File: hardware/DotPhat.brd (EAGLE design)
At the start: 30 x 65 mm, 22 parts, among them CN1 1X4-BIG, J2 RASPBERRYPI-40-PIN-GPIO_PTH, J3 USB-MICROB, U1 ATMEGA328P-MU-QFN32, X3 S4B-ZR

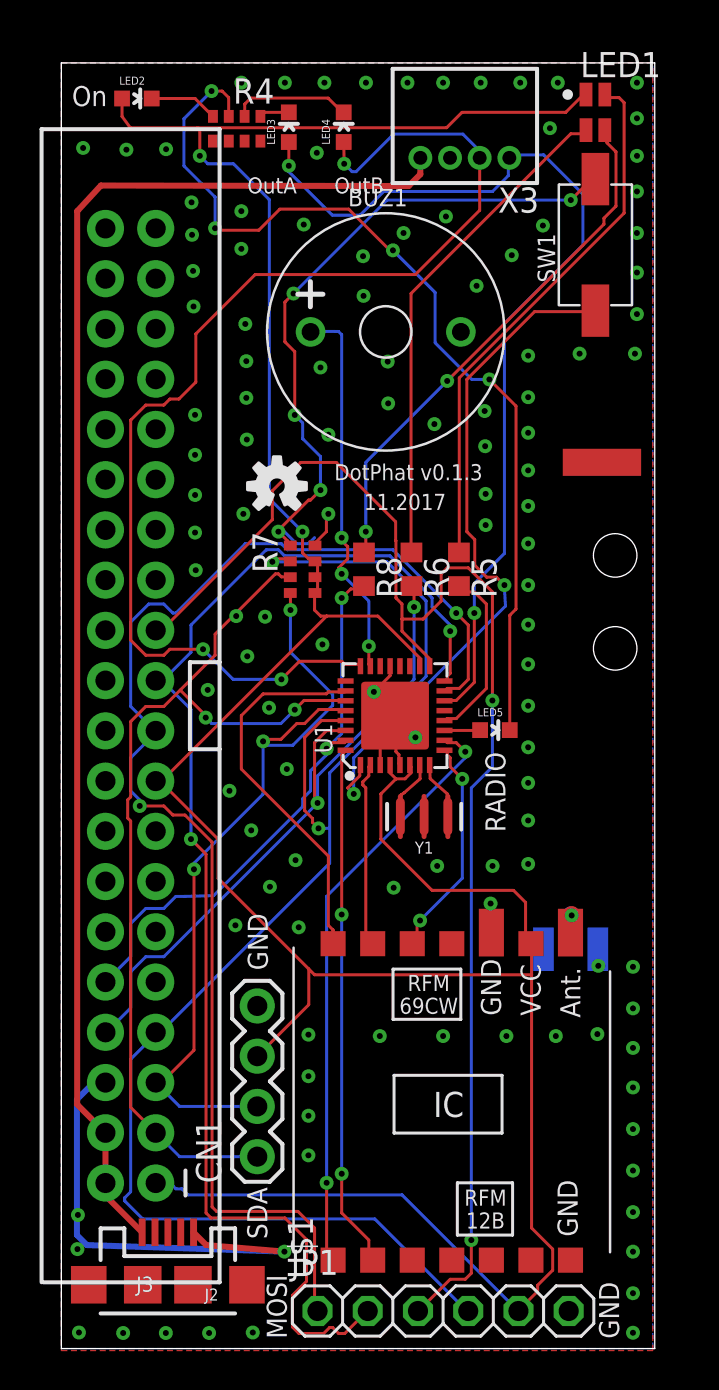
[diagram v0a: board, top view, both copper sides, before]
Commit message: Add HexId, ISM Bands
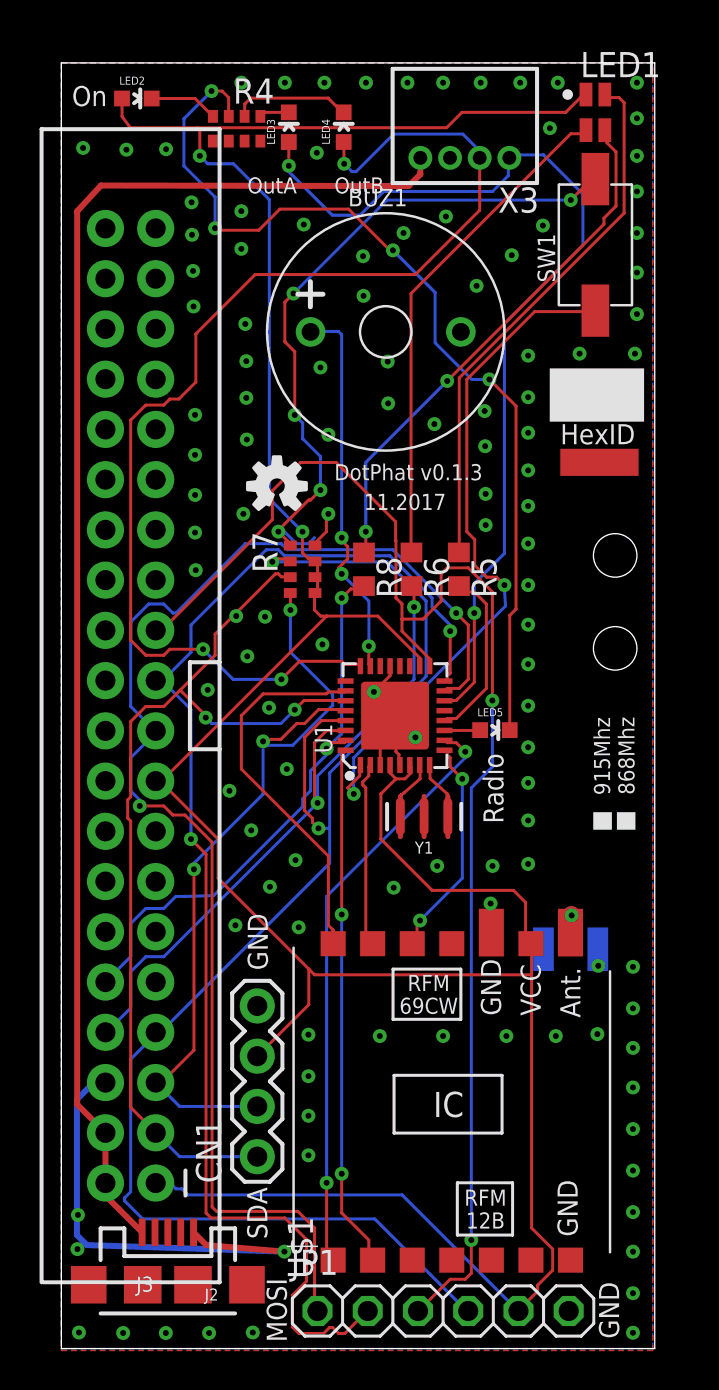
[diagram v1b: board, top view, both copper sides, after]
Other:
- board text added: "868Mhz"
- board text added: "915Mhz"
- board text added: "HexID"
- board text added: "Radio"
- board text removed: "RADIO"

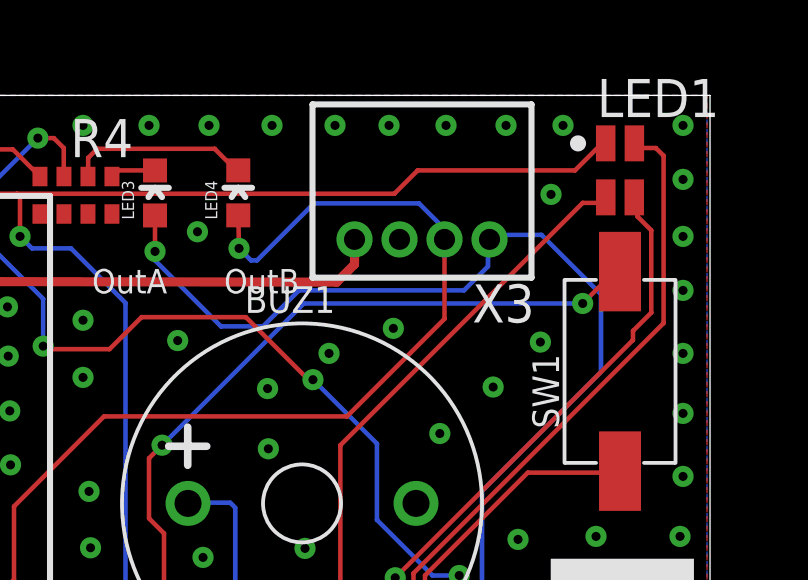
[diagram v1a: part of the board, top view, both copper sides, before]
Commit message: Make JST compatible with generic relays
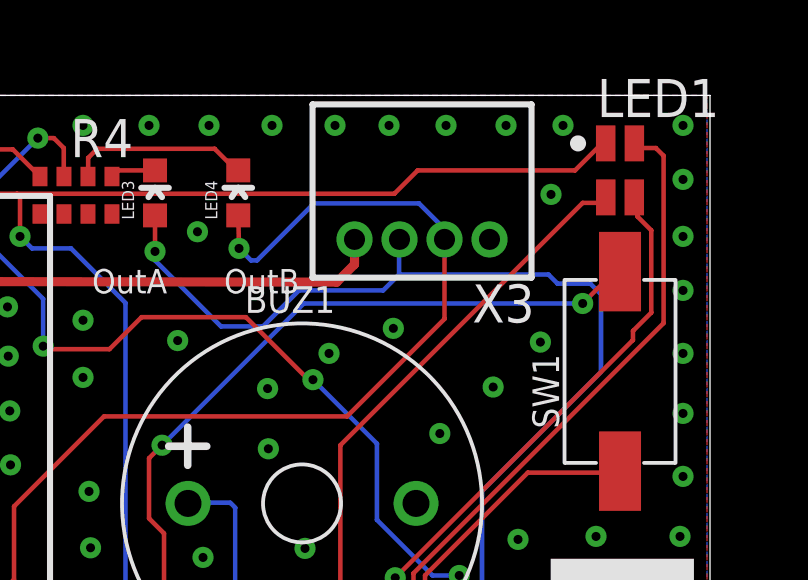
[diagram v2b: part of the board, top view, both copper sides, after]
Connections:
- net GND: now also X3.1; no longer X3.3
- net OUTA: now also X3.3; no longer X3.1

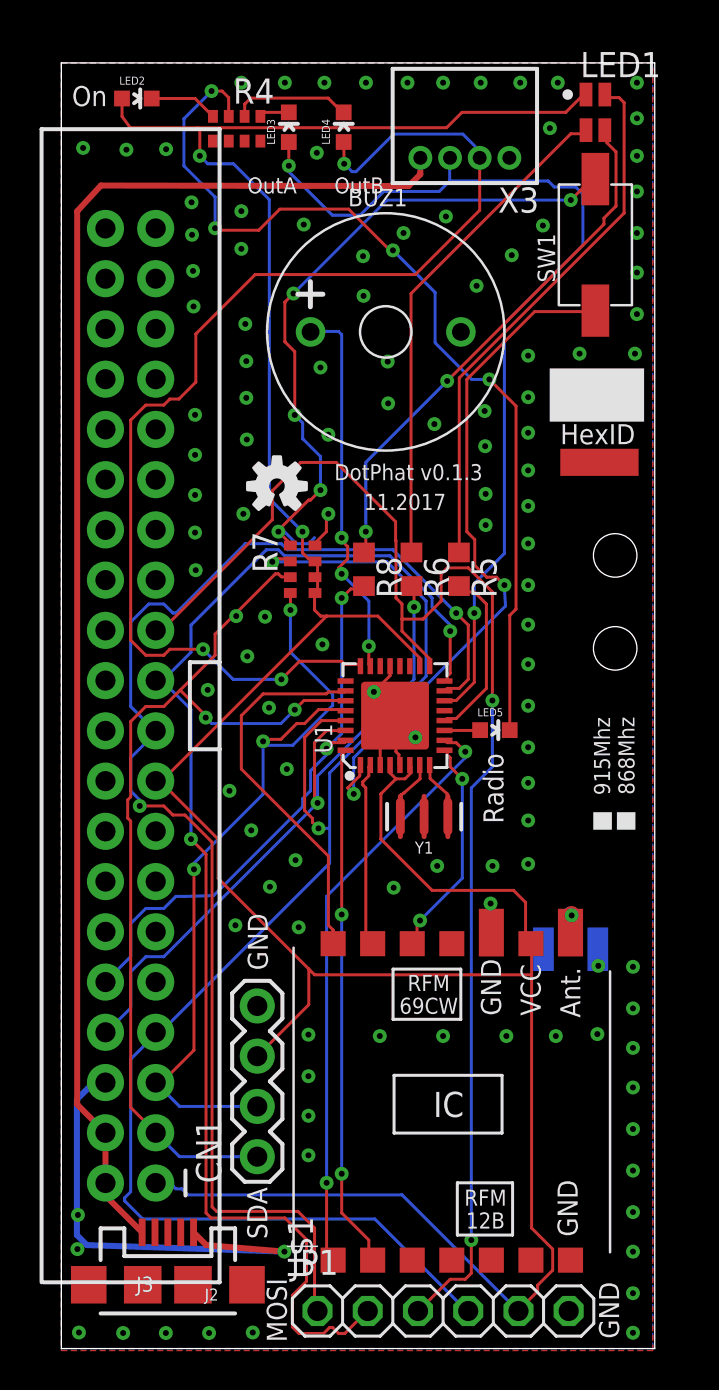
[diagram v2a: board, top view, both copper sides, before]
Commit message: Update with RPi lib with no tPlace
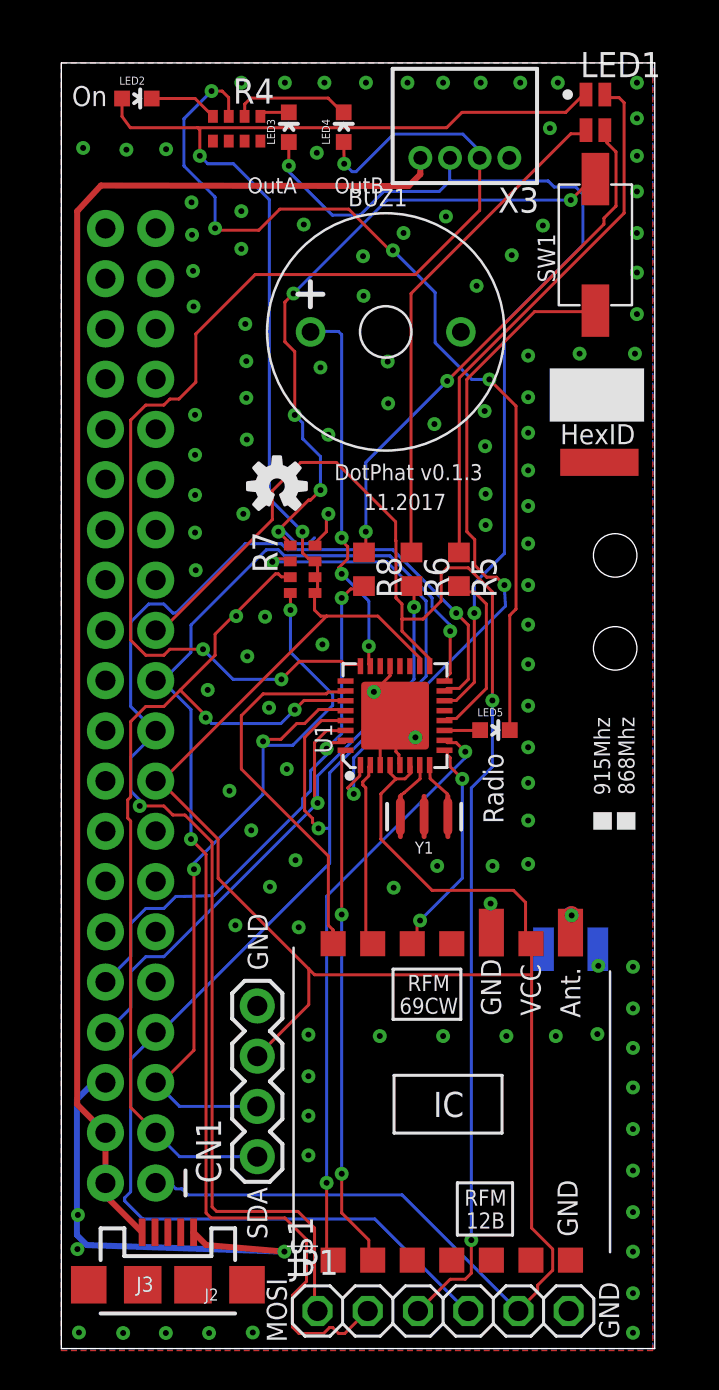
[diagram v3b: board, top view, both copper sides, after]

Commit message: Add mandatory 5V-3.3V capless regulator for USB power
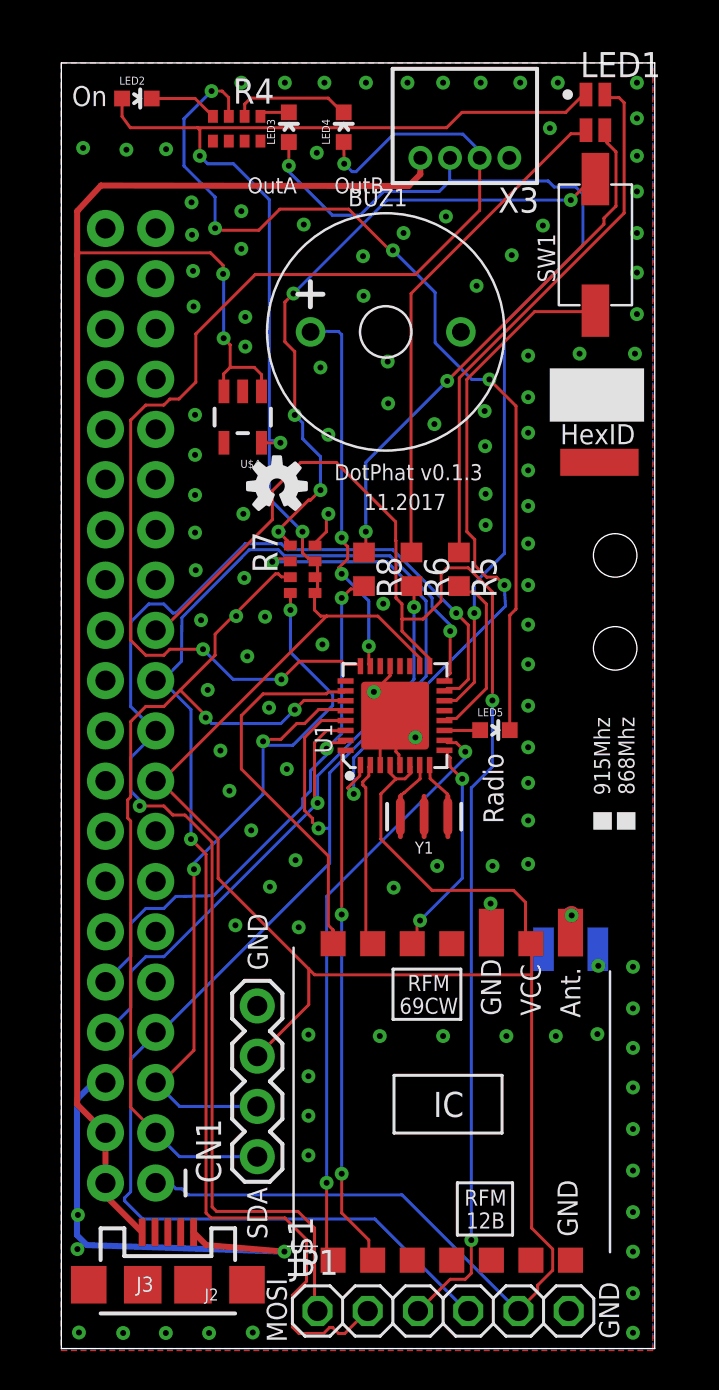
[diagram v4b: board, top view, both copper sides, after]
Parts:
- added U$4: LDCL015, LDCL015:SOT23-5
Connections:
- net +3V3: now also U$4.5
- net +5V: now also U$4.1, U$4.3
- net GND: now also U$4.2
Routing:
- net +5V: track 72.0 -> 88.9 mm, vias 0 -> 2
- net N$5: track 34.8 -> 32.9 mm
- net +3V3: track 159.6 -> 161.2 mm, vias 2 -> 3
- net GND: vias 117 -> 119

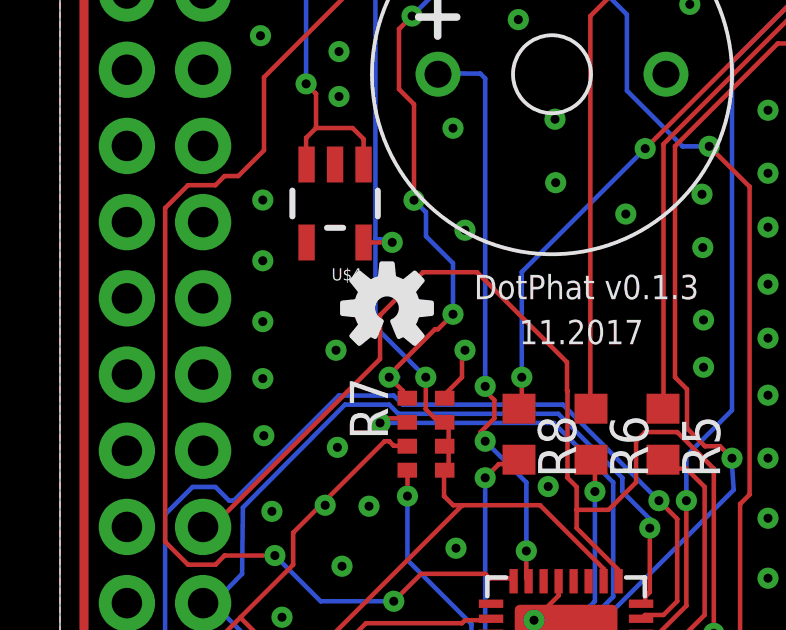
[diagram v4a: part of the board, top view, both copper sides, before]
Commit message: Add filter cap at 3.3V regulator out pin
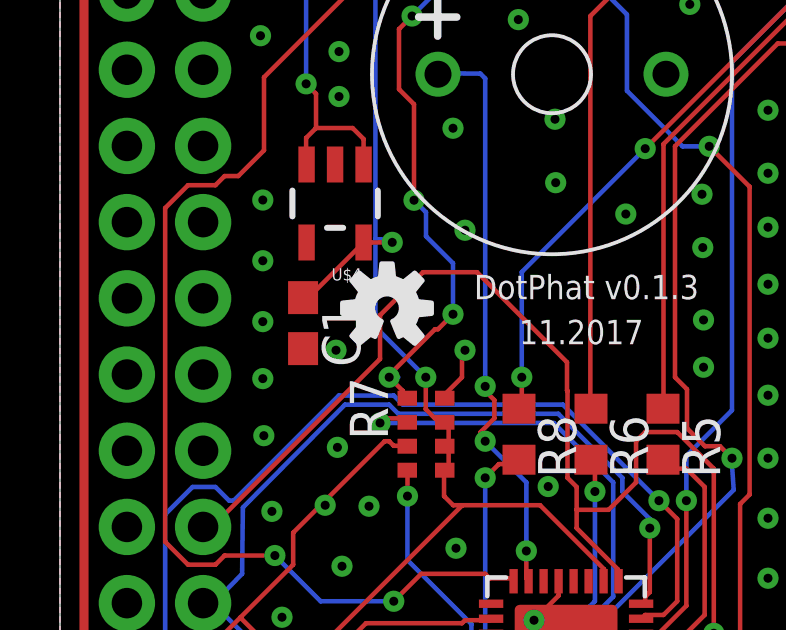
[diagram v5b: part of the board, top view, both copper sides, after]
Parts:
- added C1: (no value), rcl:C0603
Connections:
- net +3V3: now also C1.1
- net GND: now also C1.2
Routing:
- net +3V3: track 161.2 -> 164.0 mm
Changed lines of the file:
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@@
 <grid distance="1" unitdist="mil" unit="mm" style="lines" multiple="1" display="yes" altdistance="0.025" altunitdist="inch" altunit="inch"/>
 <layers>
-<layer number="1" name="Top" color="4" fill="1" visible="no" active="yes"/>
+<layer number="1" name="Top" color="4" fill="1" visible="yes" active="yes"/>
 <layer number="2" name="Route2" color="1" fill="3" visible="no" active="no"/>
 <layer number="3" name="Route3" color="4" fill="3" visible="no" active="no"/>
 <layer number="14" name="Route14" color="1" fill="6" visible="no" active="no"/>
 <layer number="15" name="Route15" color="4" fill="6" visible="no" active="no"/>
-<layer number="16" name="Bottom" color="1" fill="1" visible="no" active="yes"/>
-<layer number="17" name="Pads" color="2" fill="1" visible="no" active="yes"/>
-<layer number="18" name="Vias" color="2" fill="1" visible="no" active="yes"/>
+<layer number="16" name="Bottom" color="1" fill="1" visible="yes" active="yes"/>
+<layer number="17" name="Pads" color="2" fill="1" visible="yes" active="yes"/>
+<layer number="18" name="Vias" color="2" fill="1" visible="yes" active="yes"/>
 <layer number="19" name="Unrouted" color="6" fill="1" visible="yes" active="yes"/>
 <layer number="20" name="Dimension" color="15" fill="1" visible="yes" active="yes"/>
-<layer number="21" name="tPlace" color="7" fill="1" visible="no" active="yes"/>
-<layer number="22" name="bPlace" color="7" fill="1" visible="no" active="yes"/>
-<layer number="23" name="tOrigins" color="15" fill="1" visible="no" active="yes"/>
-<layer number="24" name="bOrigins" color="15" fill="1" visible="no" active="yes"/>
+<layer number="21" name="tPlace" color="7" fill="1" visible="yes" active="yes"/>
+<layer number="22" name="bPlace" color="7" fill="1" visible="yes" active="yes"/>
+<layer number="23" name="tOrigins" color="15" fill="1" visible="yes" active="yes"/>
+<layer number="24" name="bOrigins" color="15" fill="1" visible="yes" active="yes"/>
 <layer number="25" name="tNames" color="7" fill="1" visible="no" active="yes"/>
 <layer number="26" name="bNames" color="7" fill="1" visible="no" active="yes"/>
@@
 <element name="LED5" library="SparkFun" package="LED-0603" value="" x="21.9202" y="31.2674" rot="R270"/>
 <element name="U$4" library="LDCL015" package="SOT23-5" value="LDCL015" x="9.1694" y="47.0916" rot="R180"/>
+<element name="C1" library="rcl" package="C0603" value="" x="8.1026" y="43.1038" rot="R270"/>
 </elements>
 <signals>
@@
 <via x="9.2476" y="38.9624" extent="1-16" drill="0.3"/>
 <via x="16.2734" y="37.6574" extent="1-16" drill="0.3"/>
+<contactref element="C1" pad="2"/>
 </signal>
 <signal name="SDA">
@@
 <wire x1="11.0236" y1="45.7962" x2="11.0236" y2="45.8978" width="0.1524" layer="16"/>
 <wire x1="11.0236" y1="45.8978" x2="10.5156" y2="45.8978" width="0.1524" layer="16"/>
+<contactref element="C1" pad="1"/>
+<wire x1="8.1026" y1="43.9538" x2="8.2817" y2="43.9538" width="0.1524" layer="1"/>
+<wire x1="8.2817" y1="43.9538" x2="10.1194" y2="45.7915" width="0.1524" layer="1"/>
 </signal>
 <signal name="ADCENA">

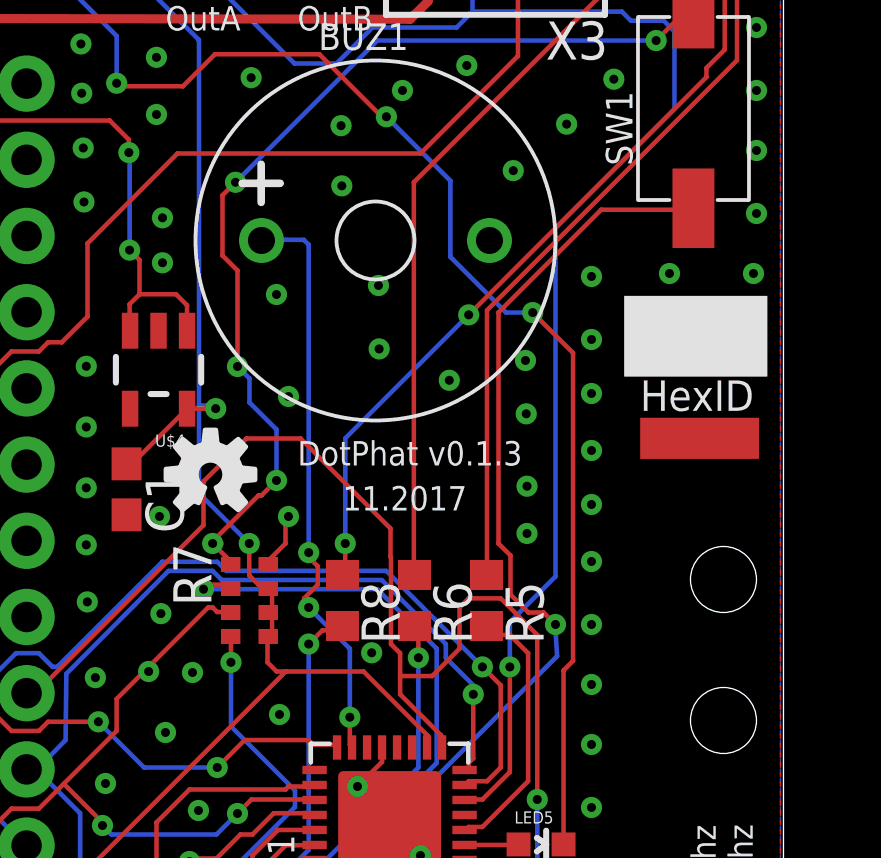
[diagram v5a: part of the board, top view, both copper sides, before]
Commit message: Replace RGB resistors for array
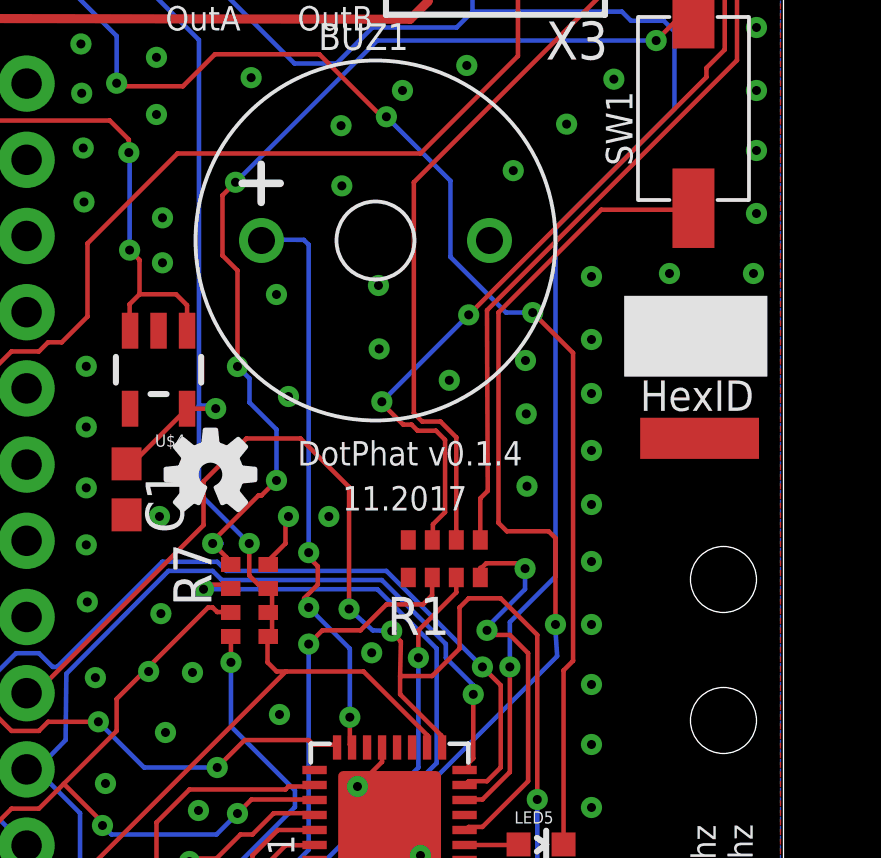
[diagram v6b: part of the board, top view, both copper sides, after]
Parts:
- removed R5, R6, R8: 67Ω, resistor:R0603
- added R1: (no value), SparkFun:0603-ARV
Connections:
- net LED: now also R1.4; no longer R5.2
- net N$1: now also R1.7; no longer R8.1
- net N$15: now also R1.5; no longer R5.1
- net N$4: now also R1.6; no longer R6.1
- net RXD: now also R1.3; no longer R6.2
- net TXD: now also R1.2; no longer R8.2
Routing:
- net LED: track 8.88 -> 13.6 mm, vias 0 -> 2
- net TXD: track 28.6 -> 32.5 mm
- net RXD: track 34.6 -> 36.7 mm
- net N$15: track 27.4 -> 26.4 mm
- net PUSH: track 35.0 -> 35.5 mm
- net SCK: track 71.1 -> 71.4 mm, vias 2 -> 4
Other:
- board text added: "DotPhat v0.1.4"
- board text removed: "DotPhat v0.1.3"
